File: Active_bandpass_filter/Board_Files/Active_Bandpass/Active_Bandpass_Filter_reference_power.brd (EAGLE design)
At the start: 100 x 80 mm, 19 parts, among them IC1 AD8542R, IC2 AD8031R, IC3 7805TV, IC4 AD8542R

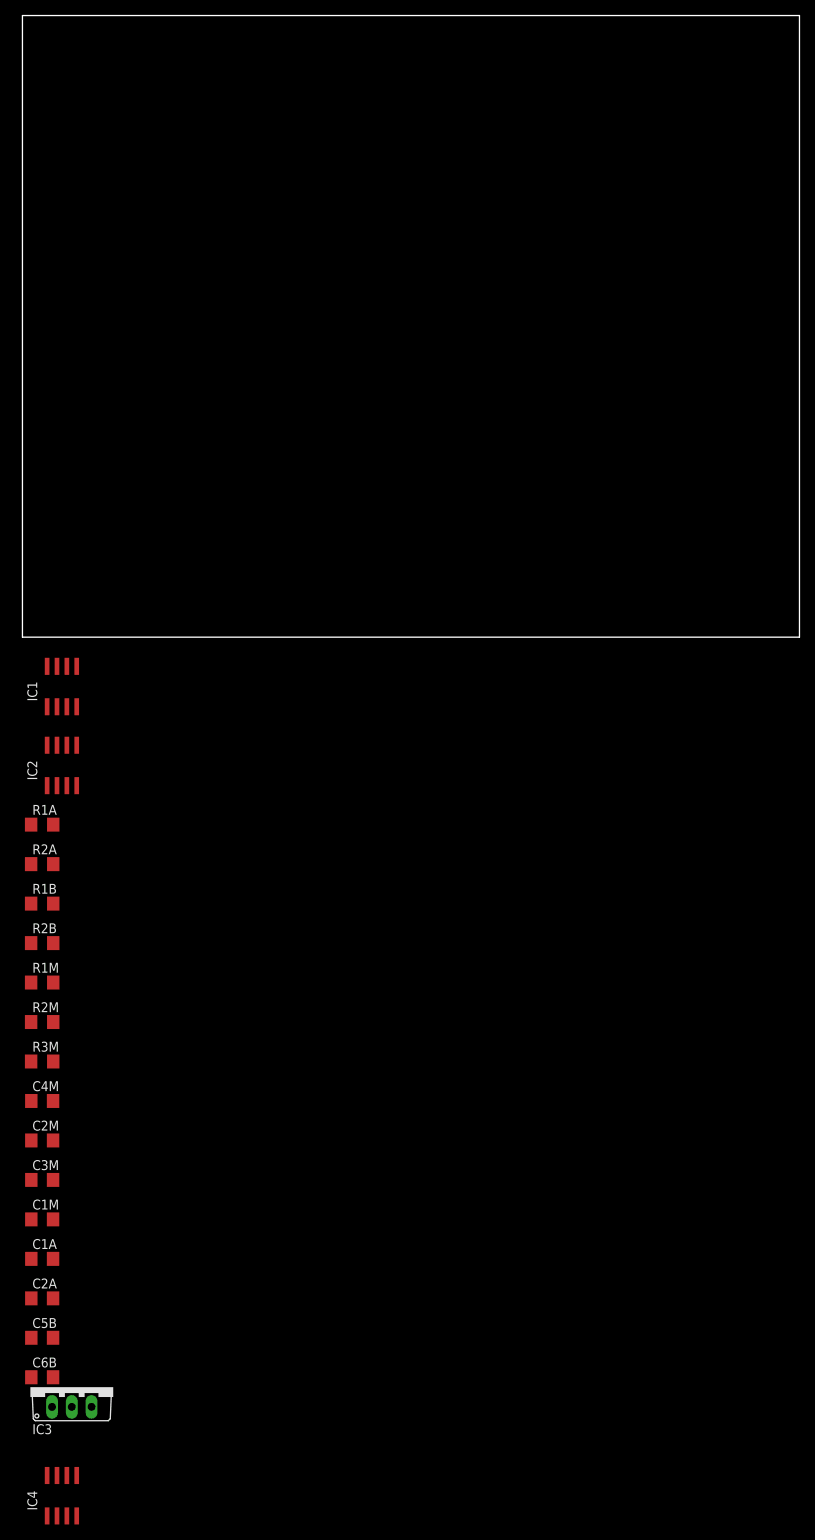
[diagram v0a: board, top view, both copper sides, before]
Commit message: split into 2 boards
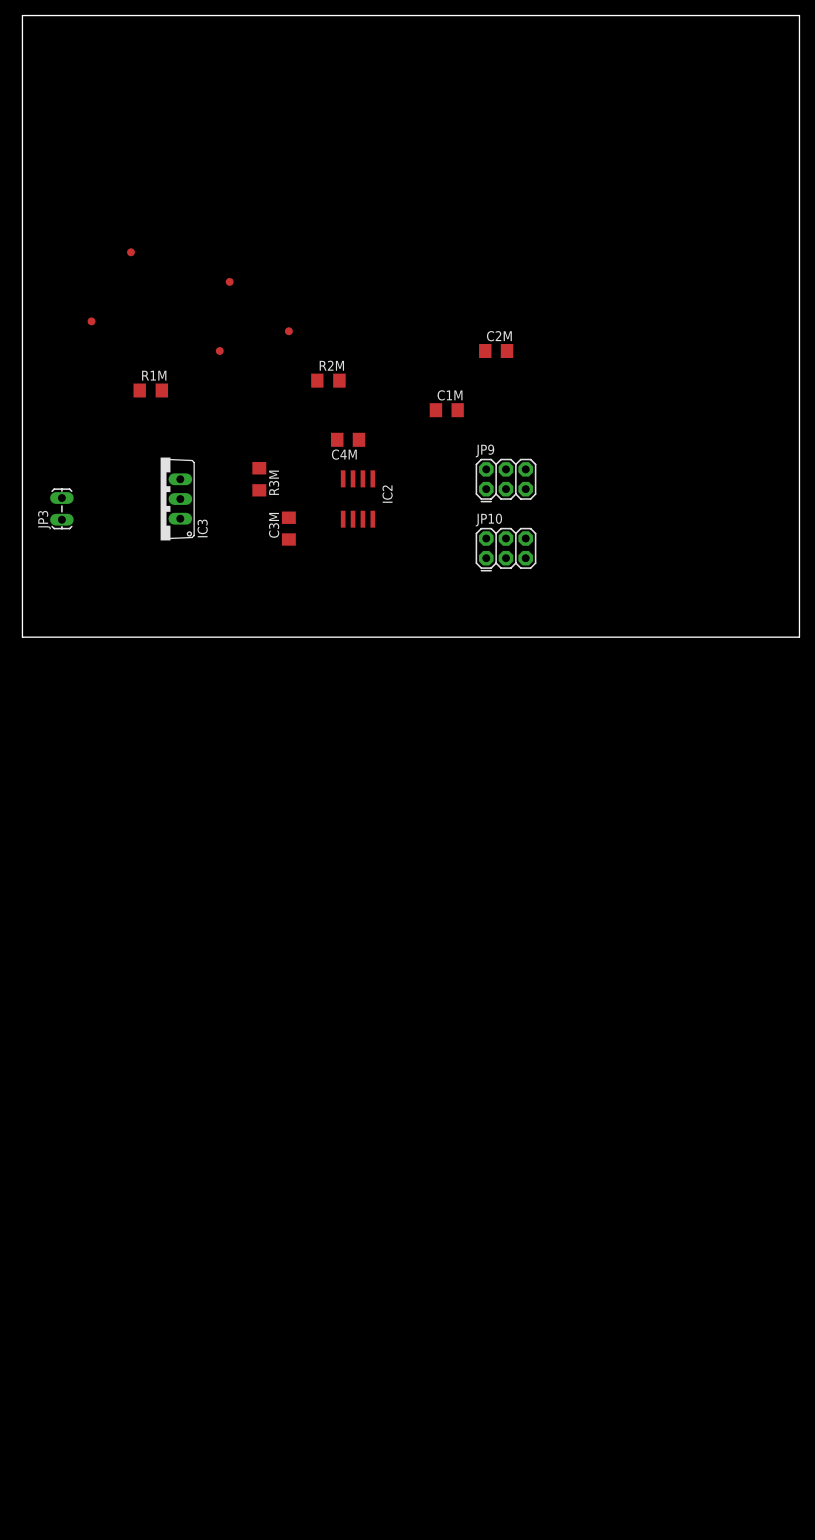
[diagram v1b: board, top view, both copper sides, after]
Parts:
- removed C1A, C2A, C5B, C6B: (no value), resistor:C1206
- removed IC1, IC4: AD8542R, analog-devices:SO8
- removed R1A, R1B, R2A, R2B: (no value), resistor:R1206
- added JP10, JP9: (no value), SparkFun-Connectors:2X3
- added JP3: (no value), SparkFun-Connectors:1X02_LOCK_LONGPADS
- added TP10, TP11, TP2, TP8, TP9: TEST-POINT3X4, SparkFun-Passives:PAD.03X.04
- C1M, C2M: value (none) -> 10uF
- C3M, C4M: value (none) -> 0.1uF
- R1M, R2M: value (none) -> 10k
- R3M: value (none) -> 4.99k
- moved C2M 117.2 mm to (61.0, 36.8)
- moved C1M 116.4 mm to (54.6, 29.2)
- moved IC3 114.9 mm to (17.8, 17.8), turned to 90 degrees
- moved C4M 93.8 mm to (41.9, 25.4), turned to 180 degrees
- moved R2M 90.4 mm to (39.4, 33.0)
- moved C3M 89.6 mm to (34.3, 14.0), turned to 90 degrees
- moved R3M 80.0 mm to (30.5, 20.3), turned to 270 degrees
- moved R1M 77.5 mm to (16.5, 31.8)
- moved IC2 51.3 mm to (43.2, 17.8), turned to 180 degrees
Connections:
- removed net N$1: C1A.1, R1A.2, R2A.1
- removed net N$2: C2A.1, IC4.3, R2A.2
- removed net N$3: C1A.2, C5B.1, IC4.1, IC4.2
- removed net N$4: C5B.2, C6B.1, R1B.1
- removed net N$5: C6B.2, IC4.5, R2B.2
- removed net SIG_IN: R1A.1
- removed net SIG_OUT: IC4.6, IC4.7, R1B.2
- removed net V+: IC1.8, IC4.8
- removed net V-: IC1.4, IC4.4
- net 5V: now also JP10.5, JP10.6, JP9.5, JP9.6, TP10.P$1, TP9.P$1
- net GND: now also JP10.3, JP10.4, JP3.2, JP9.3, JP9.4, TP11.P$1, TP8.P$1
- net REF: now also JP10.1, JP10.2, JP9.1, JP9.2, TP2.P$1; no longer C2A.2, R2B.1
- net VCC: now also JP3.1

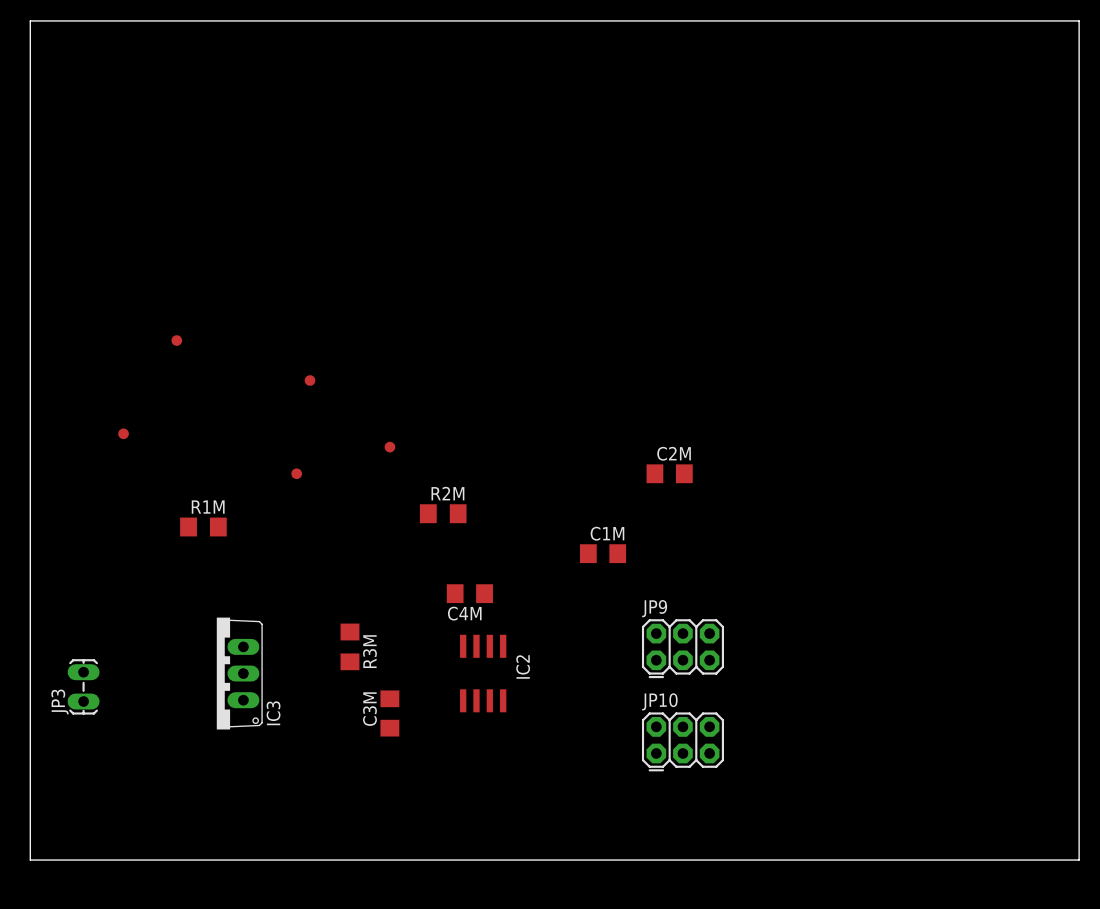
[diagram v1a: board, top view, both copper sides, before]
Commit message: first real attempt at routing power board
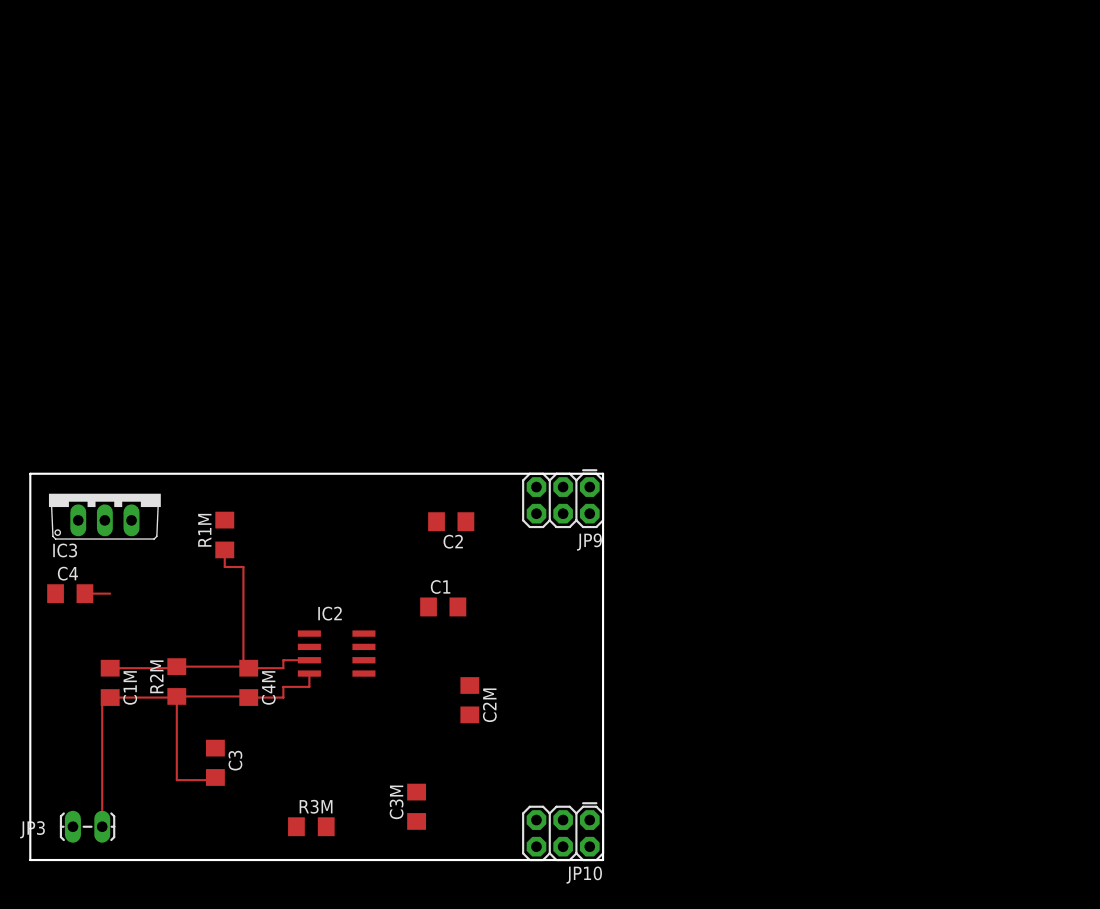
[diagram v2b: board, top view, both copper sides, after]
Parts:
- removed TP10, TP11, TP2, TP8, TP9: TEST-POINT3X4, SparkFun-Passives:PAD.03X.04
- added C1, C3: 0.1uF, resistor:C1206
- added C2, C4: 10uF, resistor:C1206
- moved C1M 48.6 mm to (7.62, 16.9), turned to 270 degrees
- moved R2M 30.0 mm to (14.0, 17.0), turned to 90 degrees
- moved C2M 28.8 mm to (41.9, 15.2), turned to 270 degrees
- moved C4M 22.7 mm to (20.8, 16.9), turned to 270 degrees
- moved IC3 20.2 mm to (7.11, 34.9), turned to 0 degrees
- moved JP9 17.7 mm to (53.3, 35.6), turned to 180 degrees
- moved R3M 17.5 mm to (26.8, 3.17), turned to 0 degrees
- moved IC2 14.1 mm to (29.2, 19.7), turned to 270 degrees
- moved JP3 12.1 mm to (4.19, 3.17), turned to 0 degrees
- moved C3M 9.25 mm to (36.8, 5.08)
- moved JP10 8.98 mm to (53.3, 3.81), turned to 180 degrees
- moved R1M 2.17 mm to (18.5, 31.0), turned to 90 degrees
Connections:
- net 5V: now also C1.2, C2.1, C3.1; no longer TP10.P$1, TP9.P$1
- net GND: now also C1.1, C2.2, C2M.1, C3.2, C4.2; no longer C2M.2, TP11.P$1, TP8.P$1
- net REF: now also C2M.2; no longer C2M.1, TP2.P$1
- net VCC: now also C4.1
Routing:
- net GND: track 0.00 -> 48.9 mm
- net N$8: track 0.00 -> 33.6 mm
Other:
- board size 100 x 80 mm -> 54.6 x 36.8 mm

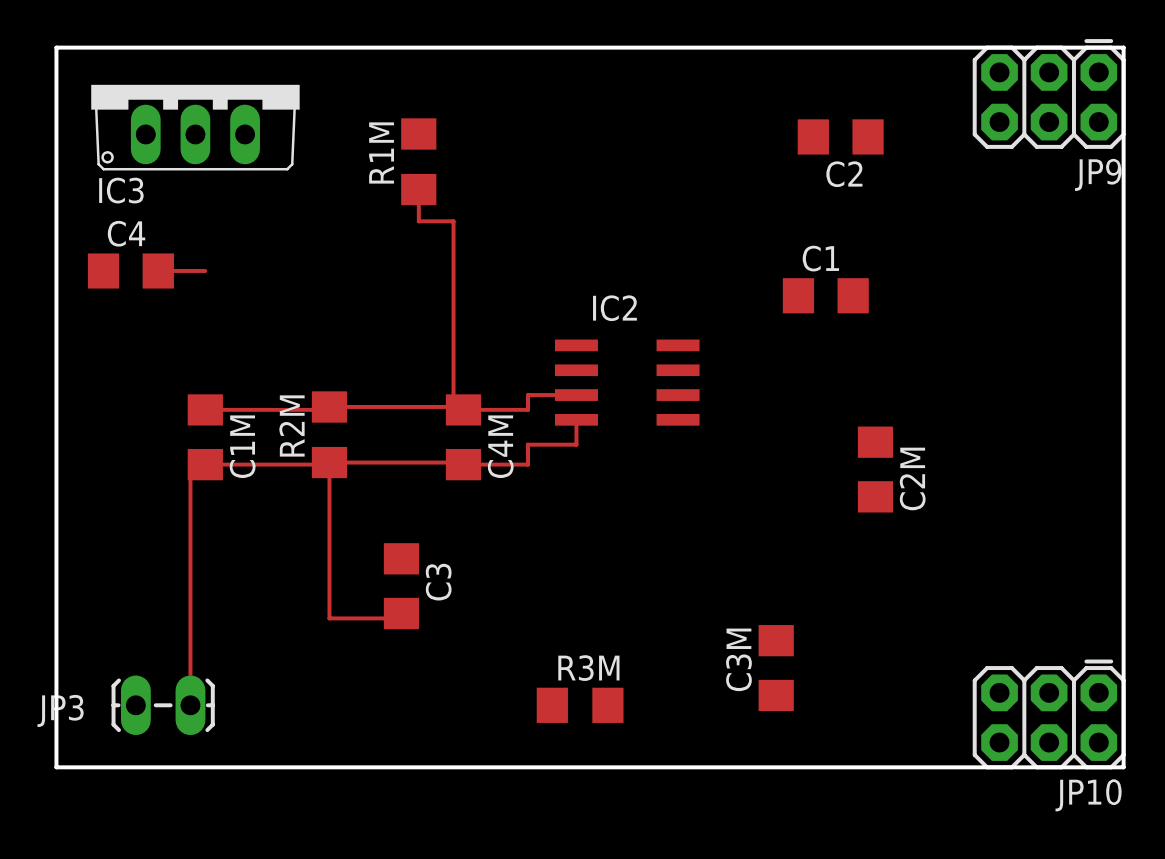
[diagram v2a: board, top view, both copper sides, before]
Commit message: reference power board routed completely
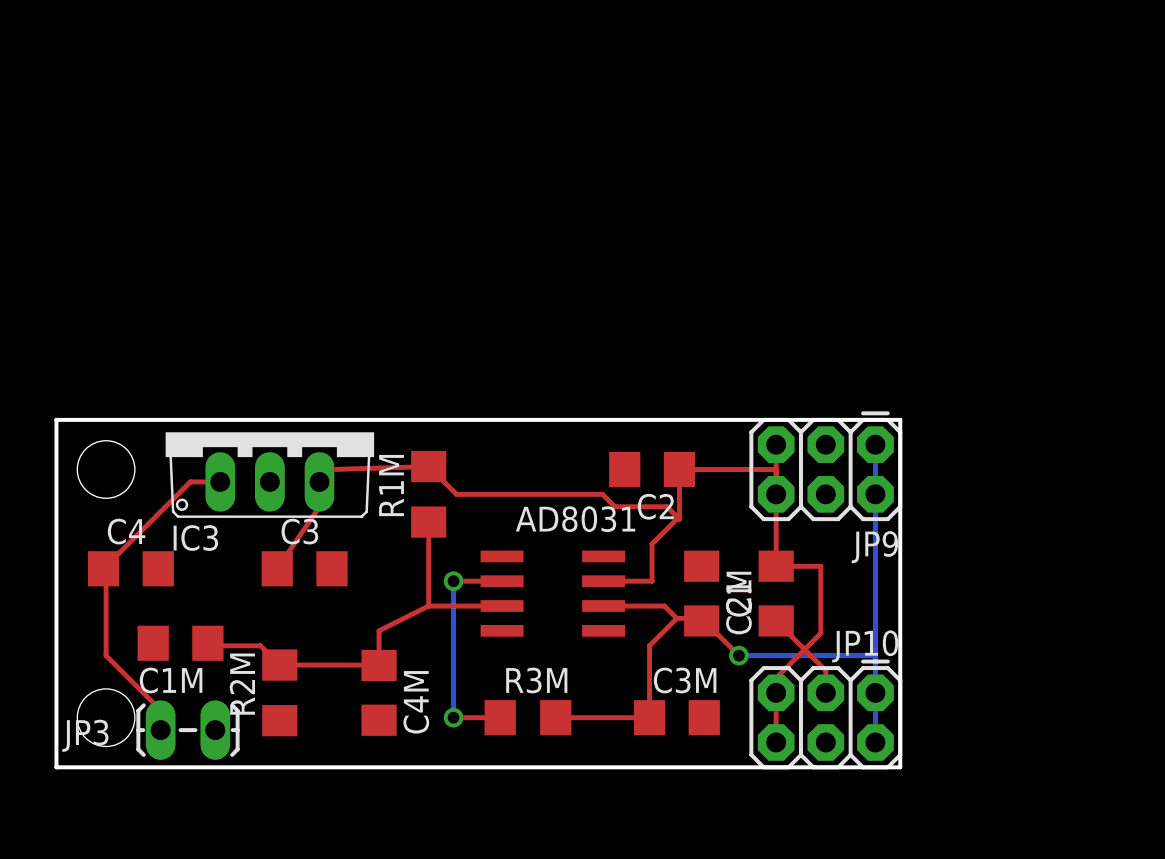
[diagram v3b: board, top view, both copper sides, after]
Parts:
- removed IC2: AD8031R, analog-devices:SO8
- added AD8031: AD8031R, analog-devices:SO8
- C2: value 10uF -> (none)
- moved JP9 22.2 mm to (41.9, 16.5)
- moved C2 19.6 mm to (30.5, 15.2)
- moved IC3 18.2 mm to (10.9, 17.1)
- moved R1M 17.0 mm to (19.1, 14.0)
- moved C1 15.5 mm to (36.8, 8.89), turned to 90 degrees
- moved C4 15.2 mm to (3.81, 10.2)
- moved C4M 13.8 mm to (16.5, 3.81)
- moved R2M 13.5 mm to (11.4, 3.81)
- moved JP10 11.4 mm to (41.9, 3.81)
- moved C2M 10.9 mm to (33.0, 8.89)
- moved C1M 10.6 mm to (6.35, 6.35), turned to 180 degrees
- moved C3M 5.68 mm to (31.8, 2.54), turned to 0 degrees
- moved C3 5.03 mm to (12.7, 10.2), turned to 0 degrees
- moved R3M 2.74 mm to (24.1, 2.54)
- moved JP3 1.80 mm to (5.46, 1.91)
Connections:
- net 5V: now also AD8031.7; no longer IC2.7
- net GND: now also AD8031.4; no longer IC2.4
- net N$12: now also AD8031.2; no longer IC2.2
- net N$8: now also AD8031.3; no longer IC2.3
- net REF: now also AD8031.6; no longer IC2.6
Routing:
- net 5V: track 0.00 -> 58.4 mm
- net GND: track 48.9 -> 4.73 mm
- net REF: track 0.00 -> 40.7 mm, vias 0 -> 1
- net VCC: track 0.00 -> 17.3 mm
- net N$12: track 0.00 -> 11.9 mm, vias 0 -> 2
- net N$8: track 33.6 -> 22.0 mm
- added copper zone on layer 1, net GND
- added copper zone on layer 16, net GND
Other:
- board size 54.6 x 36.8 mm -> 43.2 x 17.8 mm

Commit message: routing, DRC, Ratsnest all okay
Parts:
- moved JP3 0.38 mm to (5.84, 1.91)
- turned C1 to 270 degrees
- renumbered C1M to C5, C2M to C7, C3M to C8, C4M to C6, R1M to R1, R2M to R2, R3M to R3
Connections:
- net N$8 renamed C5
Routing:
- net GND: track 4.73 -> 1.14 mm
- net 5V: track 58.4 -> 59.8 mm
- net C5: track 22.0 -> 21.4 mm
